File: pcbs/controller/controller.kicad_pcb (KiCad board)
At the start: 2 copper layers, 4 parts, among them J1 Conn_01x11, J2 Conn_01x02, J3 Conn_01x02, U1 XIAO-nRF52840-SMD

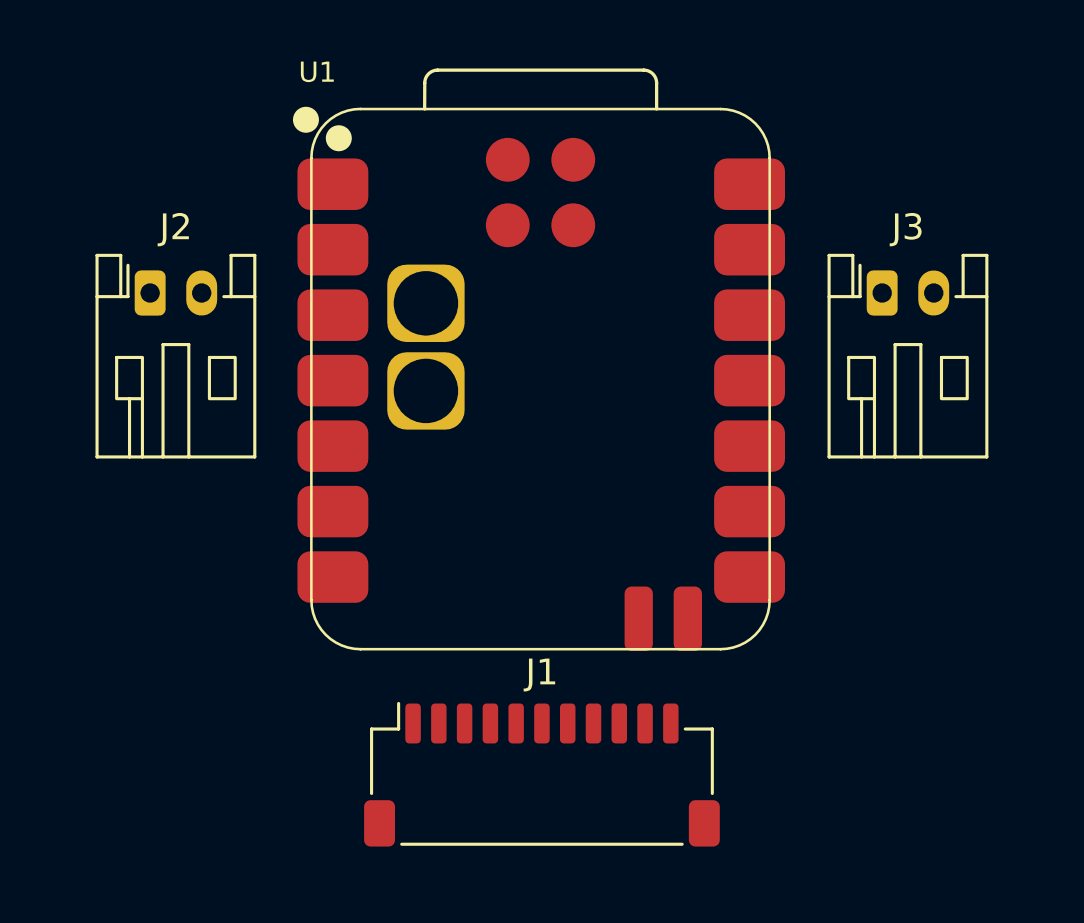
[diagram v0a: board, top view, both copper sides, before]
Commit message: Lay out the controller board and add a printable test board
The controller board outline now comes from the case model with all
corners rounded to R1.0, and is imported into the KiCad board's
Edge.Cuts with the board origin (the centre of the straight back edge)
at (100, 90), which is also the grid and aux origin, so KiCad shows the
same coordinates as the exported DXF.

- Four M2 mounting holes (board-only footprints) at the lid standoffs
- U1: the XIAO's USB-C end on the straight back edge, centred
- J1: just in front of the XIAO, centred, so the cable offset to the
  matrix connector is the same for both halves
- J2 / J3: battery connectors in the strips beside the XIAO, entry
  facing the front, so the plug and leads go into the empty front
  corner notch instead of the gap to the battery

controller_test_board.py builds a printable test board from the same
outline, drilling the holes read from KiCad's drill export (enlarged
for printing), plus the XIAO / USB-C dummy. The hole-less mock in
bay.py is replaced by xiao_mock(), and the case preview now models the
board with edges perpendicular to the lid.

Co-Authored-By: Claude Opus 5.5 <noreply@anthropic.com>
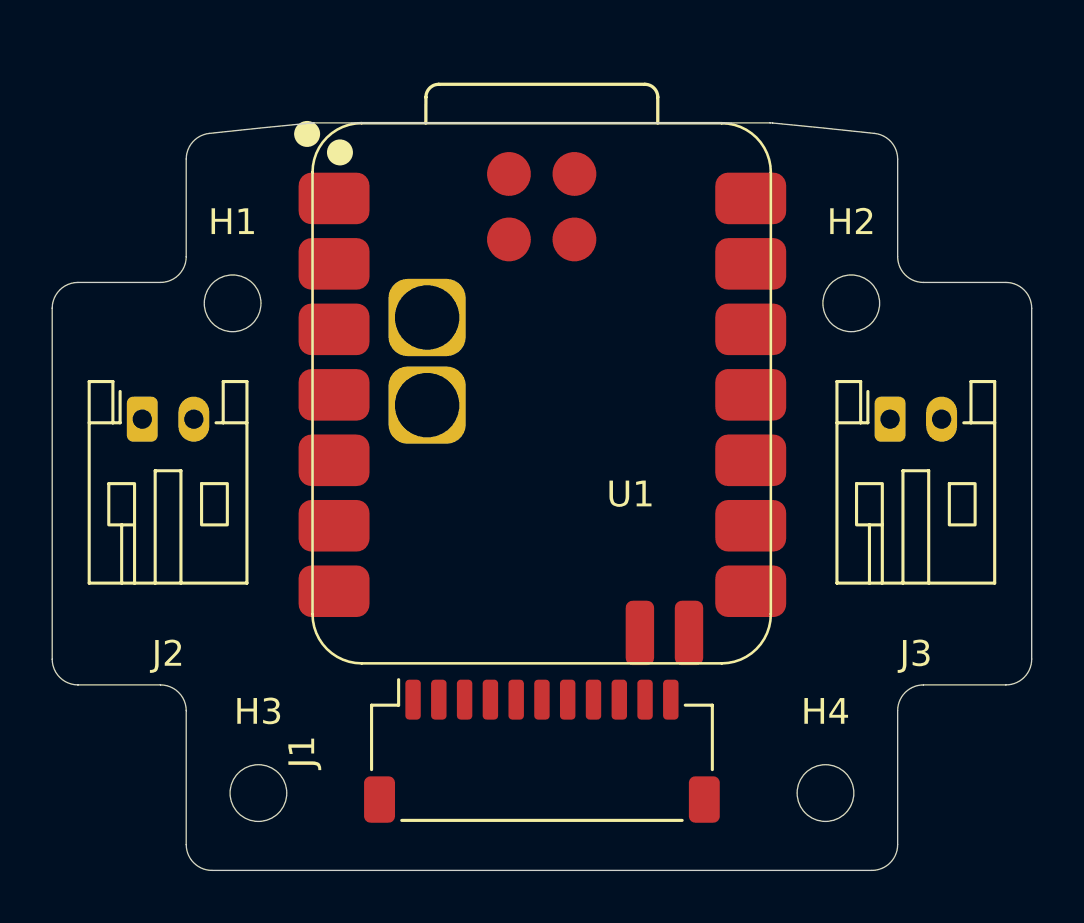
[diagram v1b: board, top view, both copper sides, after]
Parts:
- added H1: MountingHole_2.2mm_M2, MountingHole_2.2mm_M2, F.Cu at (88.0, 97.0)
- added H2: MountingHole_2.2mm_M2, MountingHole_2.2mm_M2, F.Cu at (112.0, 97.0)
- added H3: MountingHole_2.2mm_M2, MountingHole_2.2mm_M2, F.Cu at (89.0, 116.0)
- added H4: MountingHole_2.2mm_M2, MountingHole_2.2mm_M2, F.Cu at (111.0, 116.0)
- moved J2 4.90 mm to (84.5, 101.5)
- moved J3 4.90 mm to (113.5, 101.5)
- moved J1 0.92 mm to (100.0, 114.4)
- moved U1 0.55 mm to (100.0, 100.5)
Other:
- board outline added: 38 x 29 mm
